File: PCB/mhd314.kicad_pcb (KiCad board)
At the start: 4 copper layers, 65 x 56 mm, 201 parts, among them J1 Raspberry_Pi_2_3, J2 AudioJack_Pentaconn, J4 AudioJack3_SwitchTR, Q1 AO3401A, SW1 SW_Push, U1 ES9038Q2M, U10 AT24CS64-SSHM, U11 OPA1622, U13 OPA1622, U2 OPA1612AxD, U3 OPA1612AxD, U4 OPA1622, U5 LM317_SOT-223, U6 LM317_SOT-223, U7 TPS65131RGE, U8 LM317_SOT-223, U9 LM337_SOT223, Y1 ASE-50MHz

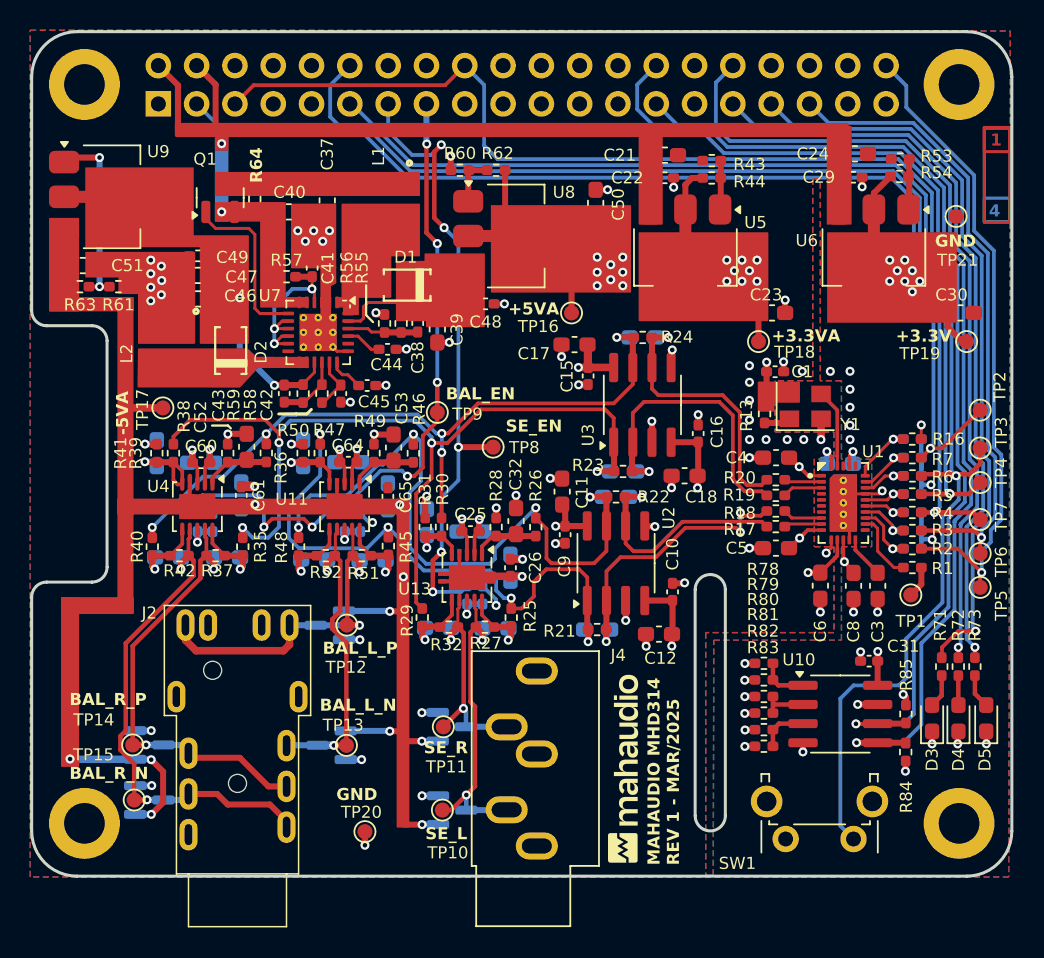
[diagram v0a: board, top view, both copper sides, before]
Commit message: Optimized designator positions and DNP for capacitors in OPA1622
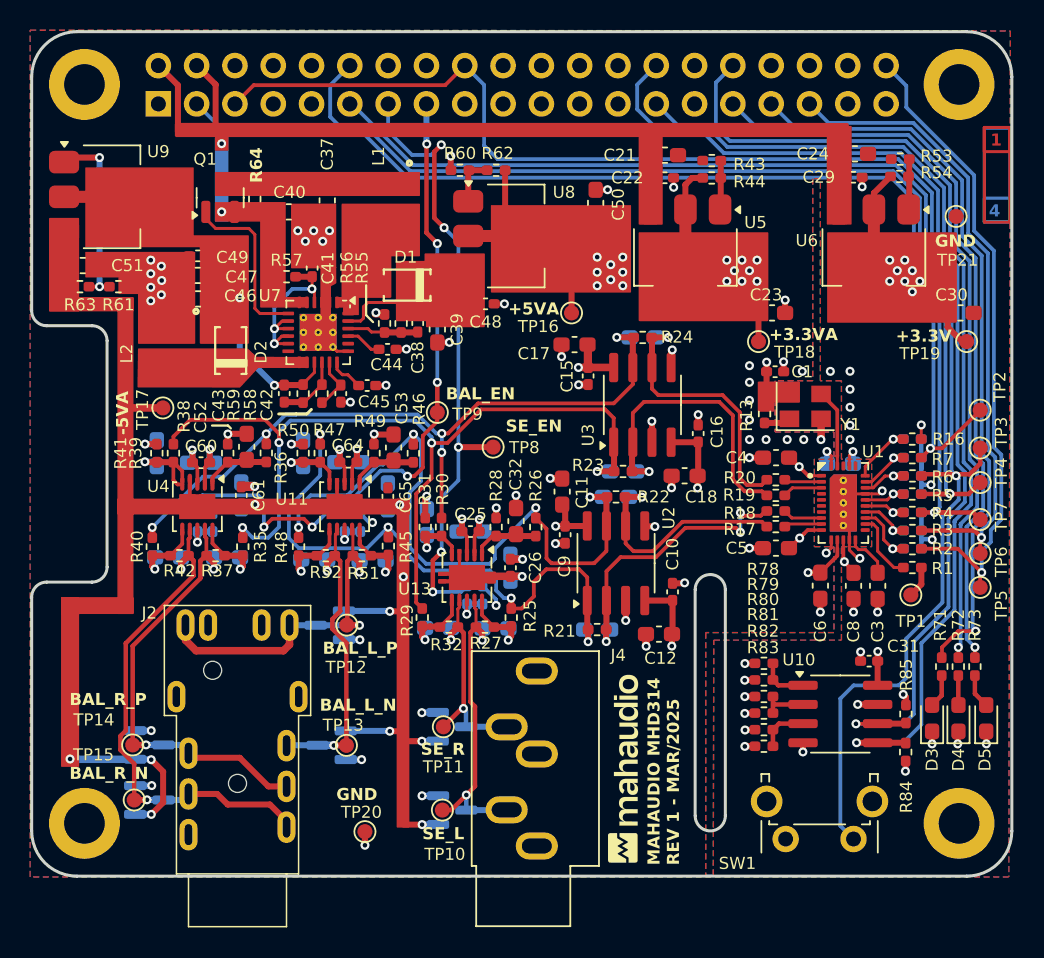
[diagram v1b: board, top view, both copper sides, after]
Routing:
- net GND: track 76.2 -> 77.8 mm, vias 86 -> 87
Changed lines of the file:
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@@
 			(layer "F.Mask"
 				(type "Top Solder Mask")
-				(color "Black")
+				(color "Green")
 				(thickness 0.01)
 			)
@@
 			(layer "B.Mask"
 				(type "Bottom Solder Mask")
-				(color "Black")
+				(color "Green")
 				(thickness 0.01)
 			)
@@
 		(tags "test point SMD pad")
 		(property "Reference" "TP10"
-			(at 0.362394 2.832194 0)
+			(at 0.162394 2.932194 0)
 			(layer "F.SilkS")
 			(effects
@@
 		(sheetname "BalDiffAmp_R")
 		(sheetfile "BalDiffAmp.kicad_sch")
-		(attr smd)
+		(attr smd dnp)
 		(fp_line
 			(start -0.146267 -0.51)
@@
 		(sheetname "SeDiffAmp")
 		(sheetfile "sediffamp.kicad_sch")
-		(attr smd)
+		(attr smd dnp)
 		(fp_line
 			(start -0.146267 0.51)
@@
 		(tags "test point SMD pad")
 		(property "Reference" "TP11"
-			(at 0.2 2.653845 0)
+			(at 0 2.653845 0)
 			(layer "F.SilkS")
 			(effects
@@
 		(sheetname "BalDiffAmp_L")
 		(sheetfile "BalDiffAmp.kicad_sch")
-		(attr smd)
+		(attr smd dnp)
 		(fp_line
 			(start -0.146267 -0.51)
@@
 		(sheetname "BalDiffAmp_L")
 		(sheetfile "BalDiffAmp.kicad_sch")
-		(attr smd)
+		(attr smd dnp)
 		(fp_line
 			(start 0.146267 -0.51)
@@
 		(sheetname "SeDiffAmp")
 		(sheetfile "sediffamp.kicad_sch")
-		(attr smd)
+		(attr smd dnp)
 		(fp_line
 			(start 0.146267 0.51)
@@
 		(sheetname "BalDiffAmp_R")
 		(sheetfile "BalDiffAmp.kicad_sch")
-		(attr smd)
+		(attr smd dnp)
 		(fp_line
 			(start 0.146267 -0.51)
@@
 		(sheetname "SeDiffAmp")
 		(sheetfile "sediffamp.kicad_sch")
-		(attr smd)
+		(attr smd dnp)
 		(fp_line
 			(start 0.146267 0.51)
@@
 		(sheetname "BalDiffAmp_R")
 		(sheetfile "BalDiffAmp.kicad_sch")
-		(attr smd)
+		(attr smd dnp)
 		(fp_line
 			(start 0.146267 0.51)
@@
 		(sheetname "BalDiffAmp_R")
 		(sheetfile "BalDiffAmp.kicad_sch")
-		(attr smd)
+		(attr smd dnp)
 		(fp_line
 			(start 0.146267 0.51)
@@
 		(sheetname "SeDiffAmp")
 		(sheetfile "sediffamp.kicad_sch")
-		(attr smd)
+		(attr smd dnp)
 		(fp_line
 			(start 0.146267 -0.51)
@@
 		(sheetname "BalDiffAmp_L")
 		(sheetfile "BalDiffAmp.kicad_sch")
-		(attr smd)
+		(attr smd dnp)
 		(fp_line
 			(start 0.146267 0.51)
@@
 		(sheetname "BalDiffAmp_L")
 		(sheetfile "BalDiffAmp.kicad_sch")
-		(attr smd)
+		(attr smd dnp)
 		(fp_line
 			(start 0.146267 0.51)
@@
 			(net 42 "unconnected-(J1-GCLK0{slash}GPIO4-Pad7)")
 			(pinfunction "GCLK0/GPIO4")
-			(pintype "bidirectional")
+			(pintype "bidirectional+no_connect")
 		)
 		(pad "8" thru_hole oval
@@
 			(net 52 "unconnected-(J1-GPIO14{slash}TXD-Pad8)")
 			(pinfunction "GPIO14/TXD")
-			(pintype "bidirectional")
+			(pintype "bidirectional+no_connect")
 		)
 		(pad "9" thru_hole oval
@@
 			(net 48 "unconnected-(J1-GPIO15{slash}RXD-Pad10)")
 			(pinfunction "GPIO15/RXD")
-			(pintype "bidirectional")
+			(pintype "bidirectional+no_connect")
 		)
 		(pad "11" thru_hole oval
@@
 			(net 53 "unconnected-(J1-GPIO23-Pad16)")
 			(pinfunction "GPIO23")
-			(pintype "bidirectional")
+			(pintype "bidirectional+no_connect")
 		)
 		(pad "17" thru_hole oval
@@
 			(net 60 "unconnected-(J1-MOSI0{slash}GPIO10-Pad19)")
 			(pinfunction "MOSI0/GPIO10")
-			(pintype "bidirectional")
+			(pintype "bidirectional+no_connect")
 		)
 		(pad "20" thru_hole oval
@@
 			(net 38 "unconnected-(J1-MISO0{slash}GPIO9-Pad21)")
 			(pinfunction "MISO0/GPIO9")
-			(pintype "bidirectional")
+			(pintype "bidirectional+no_connect")
 		)
 		(pad "22" thru_hole oval
@@
 			(net 54 "unconnected-(J1-GPIO25-Pad22)")
 			(pinfunction "GPIO25")
-			(pintype "bidirectional")
+			(pintype "bidirectional+no_connect")
 		)
 		(pad "23" thru_hole oval
@@
 			(net 50 "unconnected-(J1-SCLK0{slash}GPIO11-Pad23)")
 			(pinfunction "SCLK0/GPIO11")
-			(pintype "bidirectional")
+			(pintype "bidirectional+no_connect")
 		)
 		(pad "24" thru_hole oval
@@
 			(net 61 "unconnected-(J1-~{CE0}{slash}GPIO8-Pad24)")
 			(pinfunction "~{CE0}/GPIO8")
-			(pintype "bidirectional")
+			(pintype "bidirectional+no_connect")
 		)
 		(pad "25" thru_hole oval
@@
 			(net 55 "unconnected-(J1-~{CE1}{slash}GPIO7-Pad26)")
 			(pinfunction "~{CE1}/GPIO7")
-			(pintype "bidirectional")
+			(pintype "bidirectional+no_connect")
 		)
 		(pad "27" thru_hole oval
@@
 			(net 36 "unconnected-(J1-GCLK1{slash}GPIO5-Pad29)")
 			(pinfunction "GCLK1/GPIO5")
-			(pintype "bidirectional")
+			(pintype "bidirectional+no_connect")
 		)
 		(pad "30" thru_hole oval
@@
 			(net 58 "unconnected-(J1-GPIO16-Pad36)")
 			(pinfunction "GPIO16")
-			(pintype "bidirectional")
+			(pintype "bidirectional+no_connect")
 		)
 		(pad "37" thru_hole oval
@@
 			(net 51 "unconnected-(J1-GPIO26-Pad37)")
 			(pinfunction "GPIO26")
-			(pintype "bidirectional")
+			(pintype "bidirectional+no_connect")
 		)
 		(pad "38" thru_hole oval
@@
 			(net 45 "unconnected-(J1-GPIO20{slash}MOSI1-Pad38)")
 			(pinfunction "GPIO20/MOSI1")
-			(pintype "bidirectional")
+			(pintype "bidirectional+no_connect")
 		)
 		(pad "39" thru_hole oval
@@
 	)
 	(gr_text "SE_R"
-		(at 126.1 91.9 0)
+		(at 125.9 92 0)
 		(layer "F.SilkS" knockout)
 		(effects
@@
 	)
 	(gr_text "SE_L"
-		(at 126.2 97.6 0)
+		(at 126 97.6 0)
 		(layer "F.SilkS" knockout)
 		(effects
@@
 	)
 	(gr_text "+3.3VA"
-		(at 149.165396 64.588467 0)
+		(at 149 64.5 0)
 		(layer "F.SilkS" knockout)
 		(effects
@@
 	)
 	(segment
+		(start 154.325 78.325)
+		(end 154.325 77.65)
+		(width 0.2)
+		(layer "F.Cu")
+		(net 1)
+	)
+	(segment
 		(start 131.85 78.9325)
 		(end 132.647694 78.9325)
@@
 	)
 	(segment
+		(start 155.022708 78.873397)
+		(end 154.873397 78.873397)
+		(width 0.2)
+		(layer "F.Cu")
+		(net 1)
+	)
+	(segment
 		(start 127 64.5625)
 		(end 127.7875 64.5625)
@@
 	)
 	(segment
+		(start 154.873397 78.873397)
+		(end 154.325 78.325)
+		(width 0.2)
+		(layer "F.Cu")
+		(net 1)
+	)
+	(segment
 		(start 126.2 76.2025)
 		(end 126.2 74.848652)
@@
 	)
 	(via
+		(at 155.022708 78.873397)
+		(size 0.6)
+		(drill 0.3)
+		(layers "F.Cu" "B.Cu")
+		(net 1)
+	)
+	(via
 		(at 141.429273 76.767334)
 		(size 0.6)
@@
 	)
 	(segment
-		(start 156.224055 79.698699)
-		(end 156.098699 79.698699)
-		(width 0.25)
+		(start 154.725 78.080715)
+		(end 154.944285 78.3)
+		(width 0.2)
 		(layer "F.Cu")
 		(net 4)
 	)
 	(segment
-		(start 154.725 77.65)
-		(end 154.725 78.196706)
+		(start 155.4 78.3)
+		(end 156.2 79.1)
 		(width 0.2)
 		(layer "F.Cu")
@@
 	)
 	(segment
-		(start 154.719849 78.319849)
-		(end 154.719849 78.201857)
+		(start 156.224055 79.698699)
+		(end 156.098699 79.698699)
 		(width 0.25)
 		(layer "F.Cu")
@@
 	)
 	(segment
-		(start 154.725 78.196706)
-		(end 154.719849 78.201857)
+		(start 154.944285 78.3)
+		(end 155.4 78.3)
 		(width 0.2)
 		(layer "F.Cu")
@@
 	)
 	(segment
-		(start 156.098699 79.698699)
-		(end 154.719849 78.319849)
-		(width 0.25)
+		(start 156.2 79.1)
+		(end 156.2 79.836199)
+		(width 0.2)
+		(layer "F.Cu")
+		(net 4)
+	)
+	(segment
+		(start 154.725 77.65)
+		(end 154.725 78.080715)
+		(width 0.2)
 		(layer "F.Cu")
 		(net 4)

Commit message: Redone placement and layout of OPA1622. Still finishing touches
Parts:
- removed C27, C28, C62, C63, C66, C67: 1uF, Capacitor_SMD:C_0603_1608Metric_Pad1.08x0.95mm_HandSolder
- removed R74, R76: 10k, Resistor_SMD:R_0402_1005Metric_Pad0.72x0.64mm_HandSolder
- removed R75, R77: 22R, Resistor_SMD:R_0402_1005Metric_Pad0.72x0.64mm_HandSolder
- added R65: 10k, Resistor_SMD:R_0402_1005Metric_Pad0.72x0.64mm_HandSolder, F.Cu at (128.2, 67.6)
- added R66: 22R, Resistor_SMD:R_0402_1005Metric_Pad0.72x0.64mm_HandSolder, F.Cu at (127.0, 67.6)
- C11, C12, C17, C18: moved to B.Cu
- C2, C33, C34, C35, C36, C54, C55, C56, C57, R33, R34: moved to F.Cu
- moved R33 11.1 mm to (133.8, 70.9)
- moved R34 11.1 mm to (132.7, 70.9)
- moved C65 4.05 mm to (120.2, 72.8)
- moved C61 3.88 mm to (110.7, 72.8)
- moved C26 3.87 mm to (130.0, 76.1)
- moved R28 3.65 mm to (134.4, 75.7)
- moved C25 3.04 mm to (131.8, 75.5), turned to 90 degrees
- moved C12 3.03 mm to (142.8, 81.1), turned to -90 degrees
- moved R39 2.93 mm to (108.1, 74.5), turned to 0 degrees
- moved R25 2.93 mm to (134.3, 81.1), turned to 180 degrees
- moved R47 2.92 mm to (117.7, 74.4), turned to 0 degrees
- moved C18 2.84 mm to (143.9, 70.6), turned to -90 degrees
- moved TP9 2.81 mm to (125.2, 67.0)
- moved R46 2.75 mm to (124.5, 74.5), turned to 180 degrees
- moved R36 2.71 mm to (114.8, 74.5), turned to 180 degrees
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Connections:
- U11 pad 8: Net-(U11A-EN) -> /AMP/BalDiffAmp_L/BALDIFFAMP_ENABLE
- U4 pad 8: Net-(U4A-EN) -> /AMP/BalDiffAmp_L/BALDIFFAMP_ENABLE
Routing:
- net /AMP/BalDiffAmp_L/BALDIFFAMP_ENABLE: track 0.00 -> 27.3 mm, vias 0 -> 3
- net /AMP_DIFF_EN: track 45.5 -> 20.3 mm, vias 6 -> 3
- net GND: track 77.8 -> 53.0 mm, vias 87 -> 72
- net /AMP_SE_EN: track 42.3 -> 29.8 mm, vias 5 -> 3
- net +5VA: track 41.7 -> 29.8 mm, vias 19 -> 18
- net /AMP/BalDiffAmp_L/BALDIFFAMP_IN_P: track 40.3 -> 52.0 mm
- net Net-(U13A-EN): track 2.68 -> 11.9 mm, vias 1 -> 2
- net /AMP/BalDiffAmp_R/BALDIFFAMP_IN_N: track 49.7 -> 57.7 mm
- net -5VA: track 46.4 -> 38.6 mm, vias 13 -> 9
- net Net-(U11A--): track 6.28 -> 0.00 mm, vias 1 -> 0
- net Net-(U4B-+): track 6.18 -> 0.00 mm, vias 1 -> 0
- net Net-(U13B--): track 6.07 -> 0.00 mm, vias 1 -> 0
- net Net-(U11B--): track 5.45 -> 0.00 mm, vias 1 -> 0
- net Net-(U4A--): track 5.41 -> 0.00 mm, vias 1 -> 0
- net Net-(U13B-+): track 5.40 -> 0.00 mm, vias 1 -> 0
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
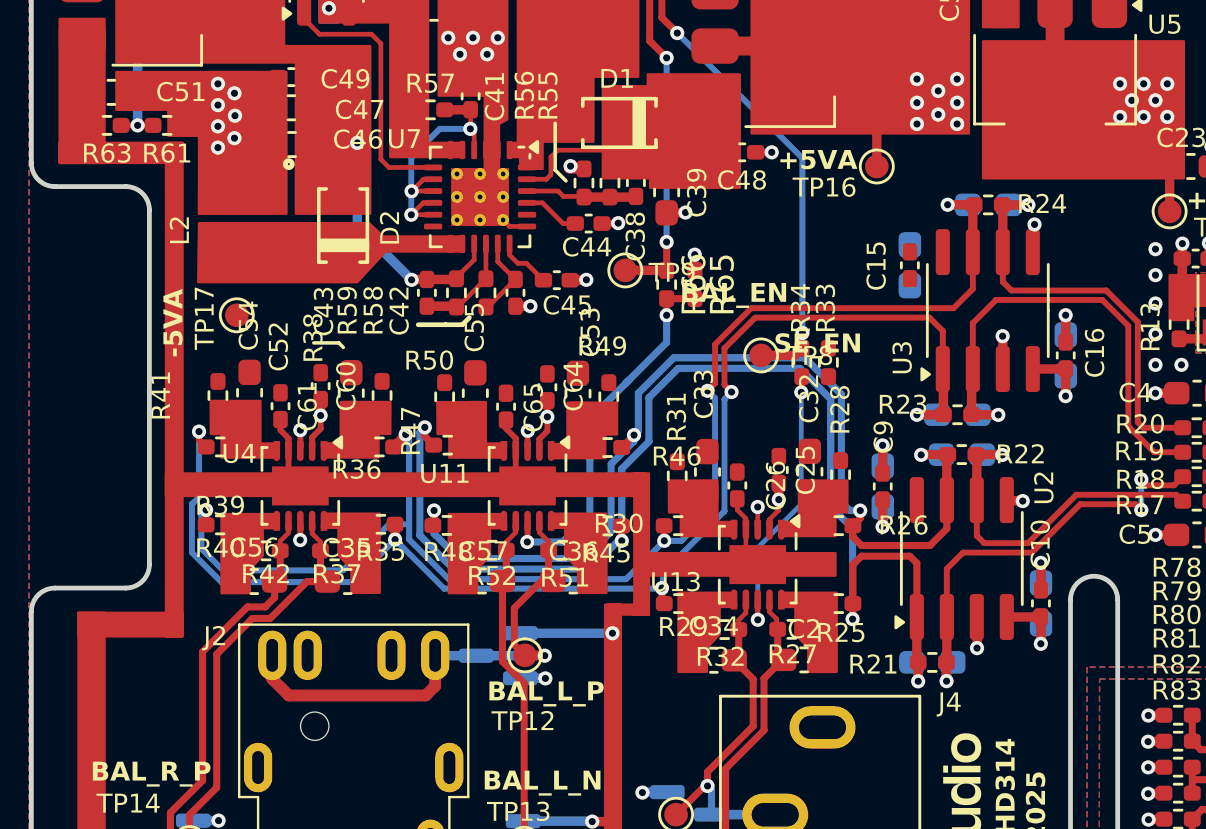
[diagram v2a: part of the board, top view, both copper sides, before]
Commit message: Finished routing with new OPA1622 layout. Pending review of designators.
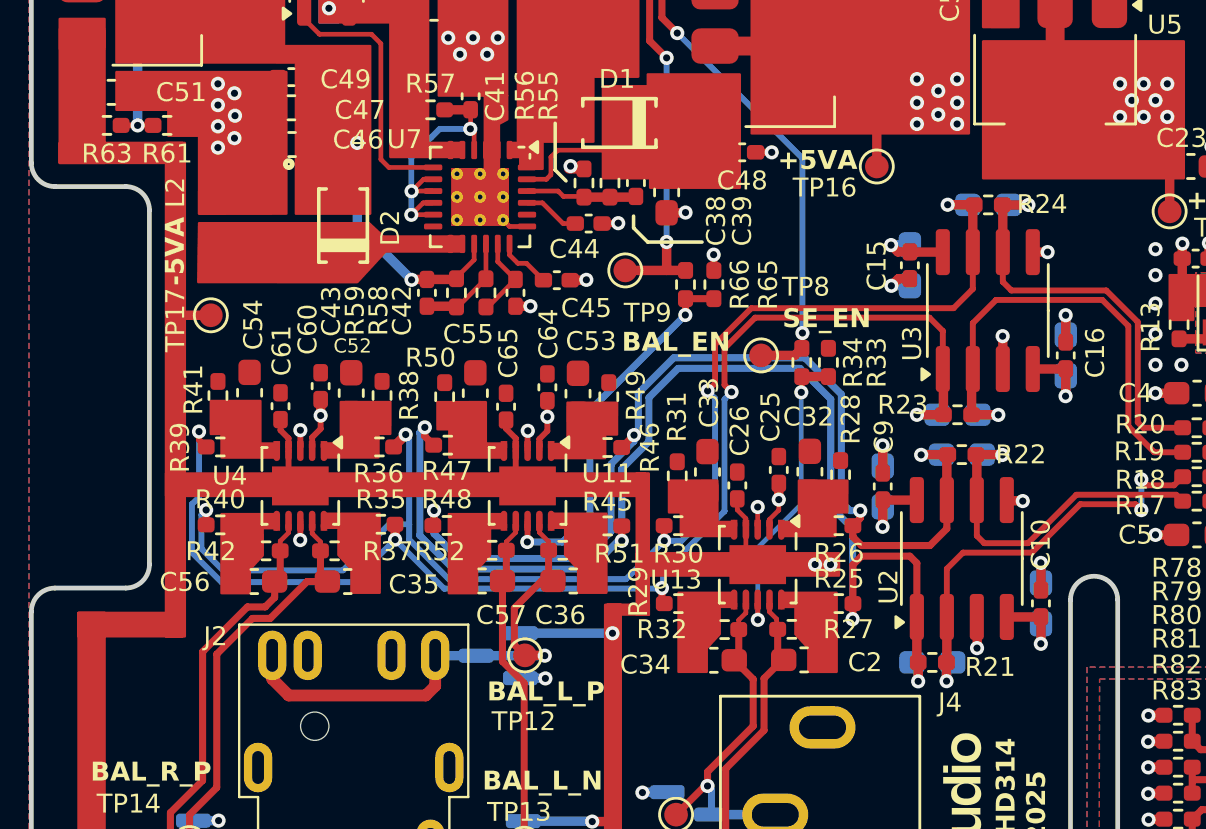
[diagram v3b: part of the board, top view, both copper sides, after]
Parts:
- moved TP17 1.10 mm to (107.7, 68.9)
- moved R65 0.80 mm to (129.0, 67.6)
- moved R66 0.80 mm to (127.8, 67.6)
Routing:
- net +5VA: track 29.8 -> 34.4 mm, vias 18 -> 19
- net -5VA: track 38.6 -> 40.1 mm, vias 9 -> 11
- net Net-(U13A-EN): track 11.9 -> 13.1 mm
- net GND: track 53.0 -> 54.2 mm, vias 72 -> 73
- net /AMP_DIFF_EN: track 20.3 -> 21.1 mm

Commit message: Optimized tracks and designators
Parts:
- moved C46 0.17 mm to (111.1, 61.5)
- moved C47 0.11 mm to (111.1, 60.0)
